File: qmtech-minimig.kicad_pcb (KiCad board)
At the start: 4 copper layers, 142.3 x 105.7 mm, 168 parts, among them IC1 ESP32-WROVER-B_(16MB), J1 DB9_Male, J10 DB23_Female_MountingHoles, J11 Conn_01x03_Male, J2 DB9_Male, J3 SCHA5B0200, J4 10118193-0001LF, J5 AUDIO-CONNECTOR-6P-SMD-344003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, J6 Mini-DIN-6, J7 Conn_02x13_Odd_Even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

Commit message: Add the missing files.
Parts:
- C11: value C -> 4u7F
- D3: footprint Diode_SMD:D_SMC -> Diode_SMD:D_SMA
- L5: footprint CDRH104RNP-220NC:INDPM102100X400N -> Inductor_SMD:L_Taiyo-Yuden_MD-4040
- SW1: value Reset ESP32 -> SW_Push
- moved C15 8.96 mm to (139.8, 136.3)
- moved C16 8.96 mm to (139.8, 138.3)
- moved JP1 8.96 mm to (147.6, 139.5)
- moved L5 5.91 mm to (134.6, 136.2)
- moved C11 4.16 mm to (104.8, 51.5), turned to 90 degrees
- moved R35 2.83 mm to (126.7, 144.1)
- moved R36 2.83 mm to (128.5, 144.1)
- moved R37 2.83 mm to (136.7, 144.2)
- moved U5 2.83 mm to (132.5, 144.0)
- moved D3 1.96 mm to (126.8, 136.0)
- moved R32 0.50 mm to (107.1, 46.8)
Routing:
- net Net-(C15-Pad1): track 32.9 -> 25.6 mm
- net VIN12V: track 130.5 -> 129.1 mm
- net VIN5V: track 224.7 -> 224.0 mm
- net ESP_SD_VCC_EN: track 60.3 -> 59.8 mm

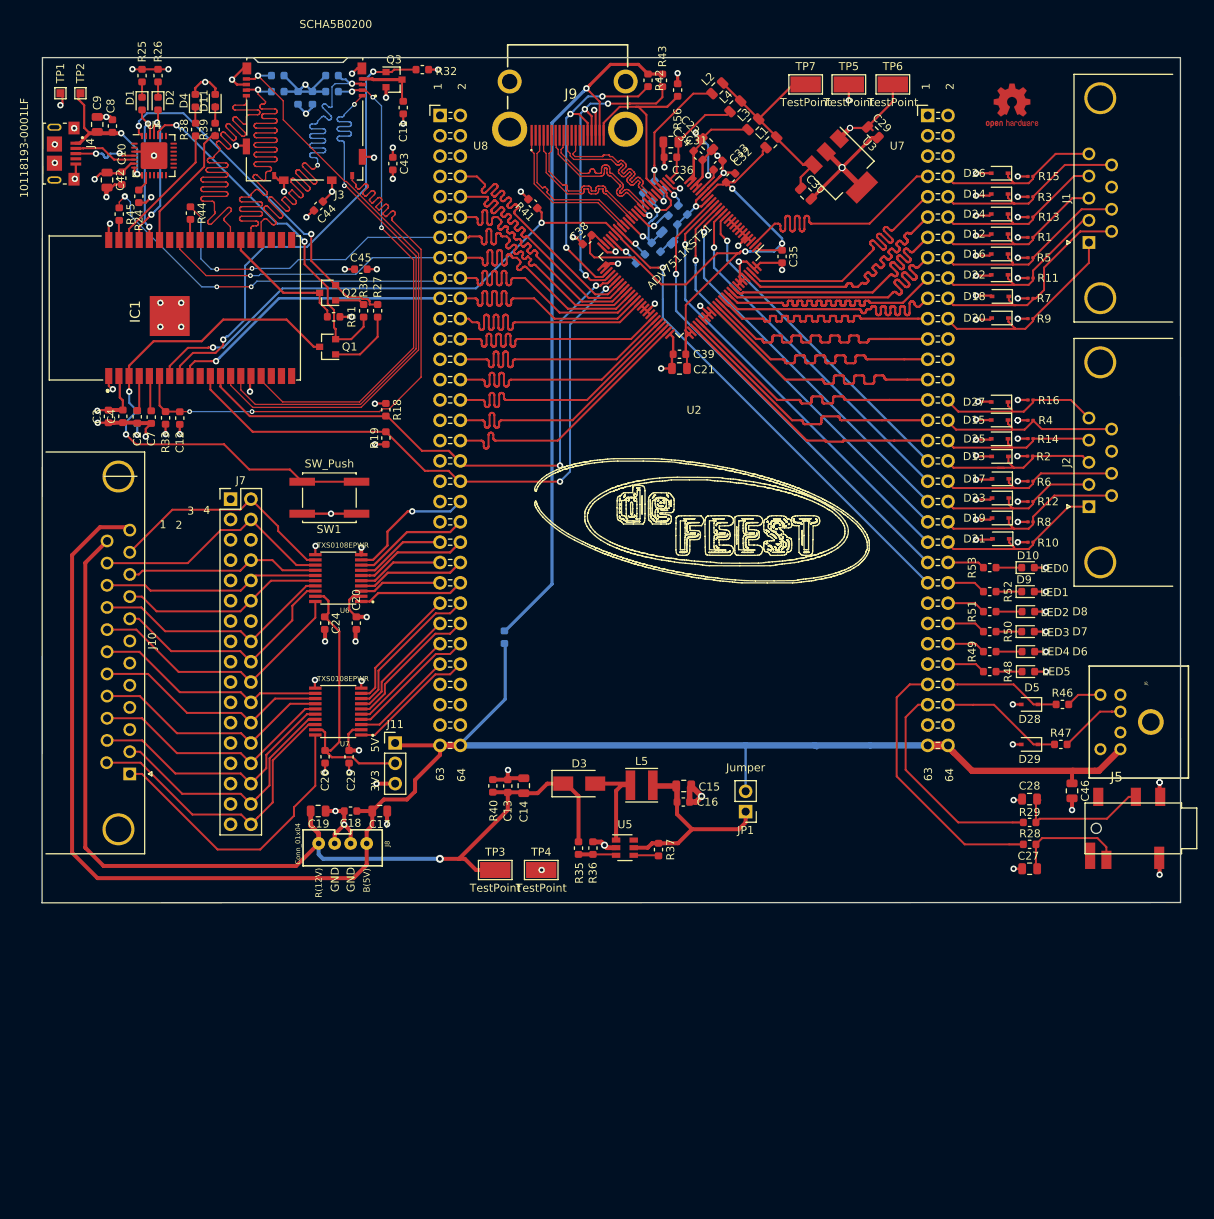
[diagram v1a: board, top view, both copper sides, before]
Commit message: Added ESD protection, and removed the curved lines around the adv7511.
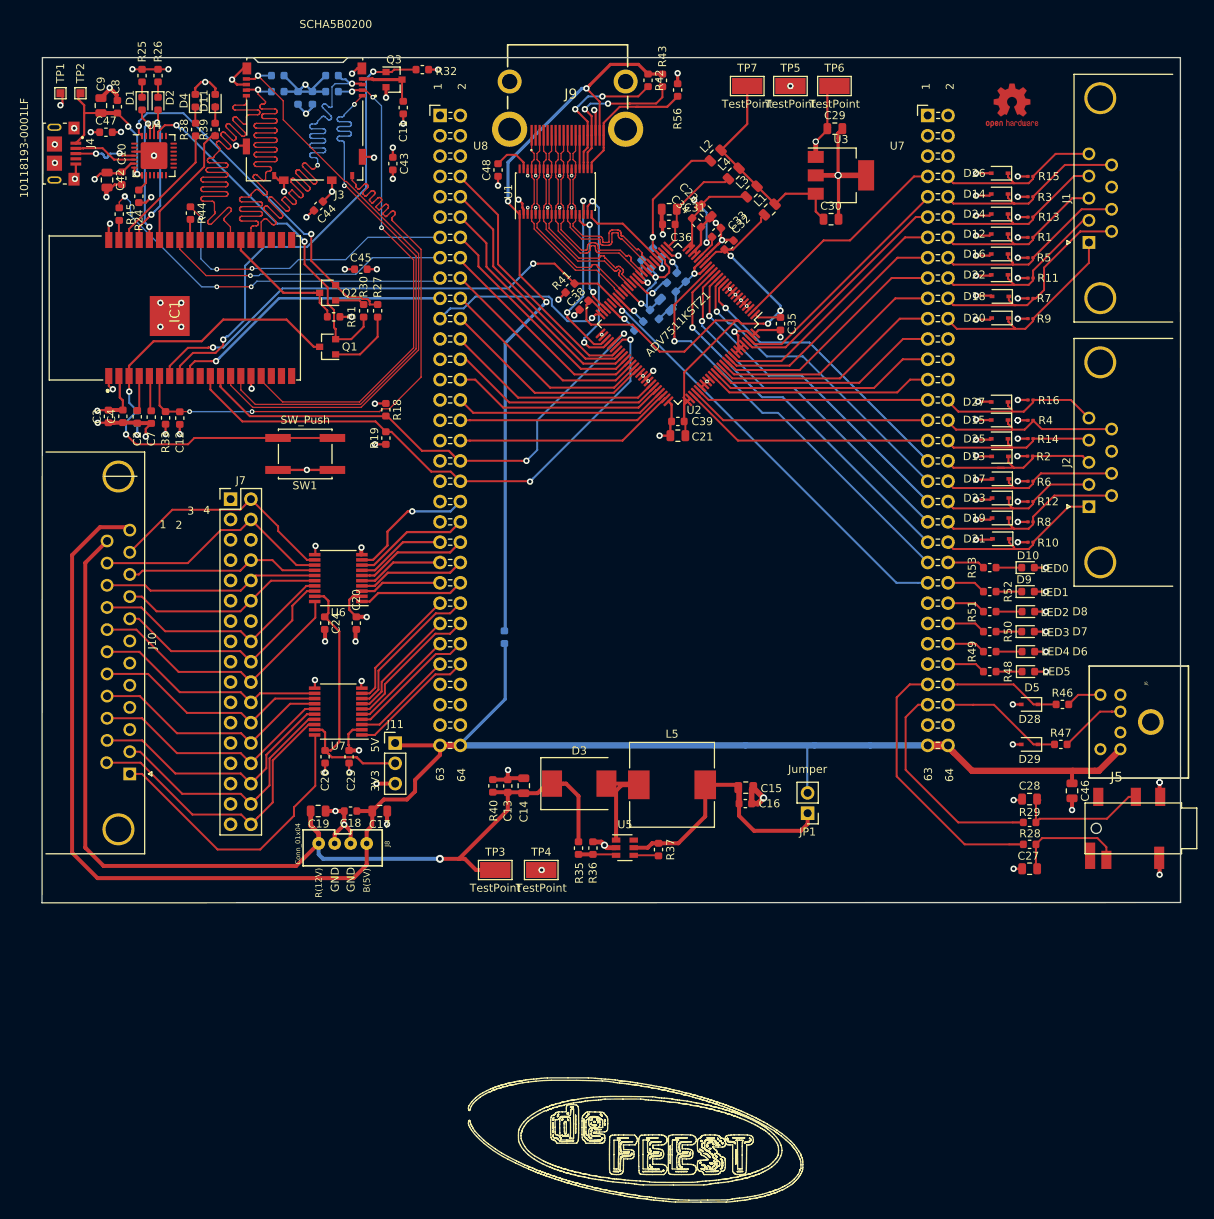
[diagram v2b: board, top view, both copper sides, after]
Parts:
- added C47: 10n, Capacitor_SMD:C_0603_1608Metric, F.Cu at (67.6, 54.6)
- added C48: 100nF, Resistor_SMD:R_0603_1608Metric, F.Cu at (116.6, 59.3)
- added U1: TPD12S520DBT, Package_SO:TSSOP-38_4.4x9.7mm_P0.5mm, F.Cu at (123.8, 62.0)
- C11: value 4u7F -> C
- D3: footprint Diode_SMD:D_SMA -> Diode_SMD:D_SMC
- L5: footprint Inductor_SMD:L_Taiyo-Yuden_MD-4040 -> Inductor_SMD:L_10.4x10.4_H4.8
- U6, U7: footprint TXS0108EPWR:SOP65P640X120-20N -> Package_SO:TSSOP-20_4.4x6.5mm_P0.65mm
- moved R41 11.5 mm to (125.6, 74.0), turned to 225 degrees
- moved C31 8.40 mm to (138.0, 64.2)
- moved C32 8.40 mm to (143.9, 67.1)
- moved C34 8.40 mm to (141.4, 65.9)
- moved C35 8.40 mm to (151.9, 78.5)
- moved C37 8.40 mm to (136.2, 77.4)
- moved C39 8.40 mm to (139.1, 90.7)
- moved L1 8.40 mm to (150.6, 64.2)
- moved L2 8.40 mm to (143.8, 57.5)
- moved L3 8.40 mm to (148.3, 62.0)
- moved L4 8.40 mm to (146.1, 59.7)
- moved R57 8.40 mm to (139.5, 72.7)
- moved C23 8.40 mm to (142.5, 64.5)
- moved C33 8.40 mm to (145.5, 68.7)
- moved C40 8.40 mm to (136.5, 69.6)
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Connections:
- net Net-(J9-Pad18) renamed /HDMI transmitter/HDMI5V
- ADV7511KSTZ1 pad 48: GND -> ADV_CEC
- ADV7511KSTZ1 pad 50: GND -> ADV_CECCLK
- J9 pad 13: Net-(J9-Pad13) -> ADV_CEC_C
- J9 pad 15: ADV_DDCSCL -> ADV_DDCSCL_C
- J9 pad 16: ADV_DDCSDA -> ADV_DDCSDA_C
- J9 pad 19: ADV_HPD -> ADV_HPD_C
- R42 pad 2: ADV_DDCSCL -> ADV_DDCSCL_C
- R43 pad 2: ADV_DDCSDA -> ADV_DDCSDA_C
- R56 pad 2: ADV_HPD -> ADV_HPD_C
- U2 pad U721: Net-(U2-PadU721) -> ADV_CECCLK
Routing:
- net ADV_CECCLK: track 0.00 -> 23.3 mm, vias 0 -> 1
- net ADV_DDCSDA_C: track 0.00 -> 19.9 mm, vias 0 -> 2
- net ADV_DDCSCL_C: track 0.00 -> 18.6 mm, vias 0 -> 2
- net ADV_HPD_C: track 0.00 -> 17.3 mm
- net ADV_DDCSDA: track 40.1 -> 24.3 mm, vias 3 -> 2
- net ADV_DDCSCL: track 39.2 -> 23.6 mm, vias 3 -> 2
- net ADV_CEC: track 0.00 -> 13.7 mm, vias 0 -> 2
- net ADV_HPD: track 24.0 -> 10.7 mm
- net ADV_INT: track 127.9 -> 118.1 mm
- net ADV_G_3: track 35.0 -> 26.6 mm
- net ADV_G_4: track 35.0 -> 26.6 mm
- net ADV_SCL: track 74.8 -> 66.5 mm
- net ADV_G_5: track 35.0 -> 27.0 mm
- net ADV_R_0: track 35.0 -> 27.1 mm
- net Net-(C15-Pad1): track 25.6 -> 33.4 mm
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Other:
- net class HDMI: clearance 0.2 -> 0.127; via_dia 0.4 -> 0.45
- rule via_min_drill: 0.3 -> 0.2
- rule via_min_size: 0.4 -> 0.45

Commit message: Add an oscillator for the CEC functionality.
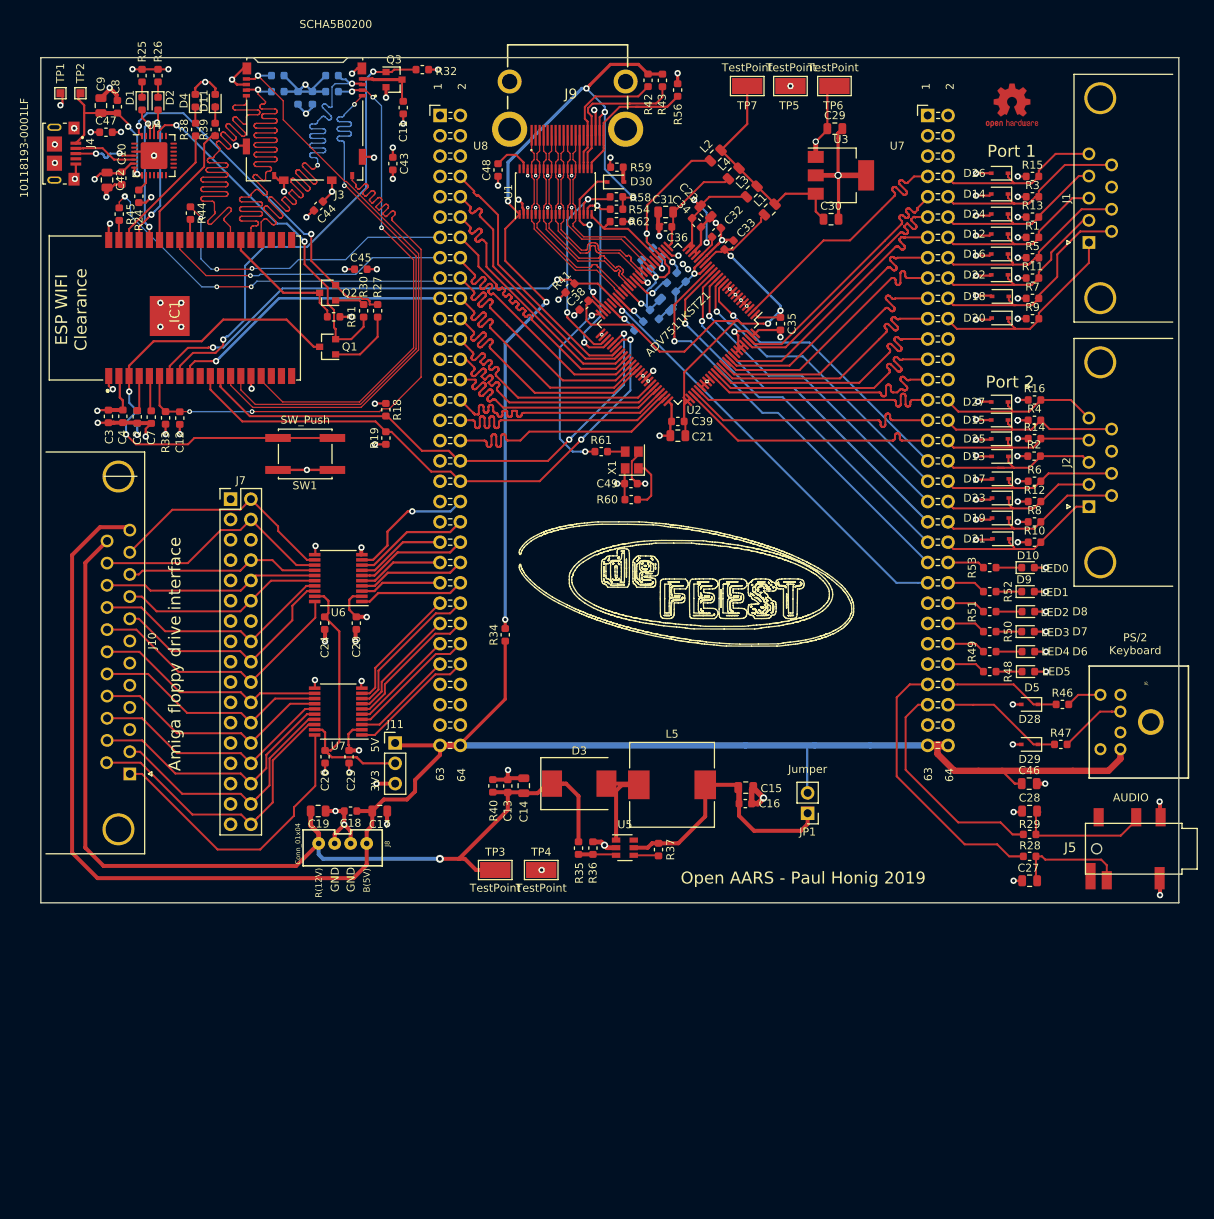
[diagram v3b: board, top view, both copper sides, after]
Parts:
- added C49: 100nF, Capacitor_SMD:C_0603_1608Metric, F.Cu at (133.2, 98.5)
- added D30: 1N4148, Diode_SMD:D_SOD-323, F.Cu at (131.3, 60.8)
- added R54: 2K, Resistor_SMD:R_0603_1608Metric, F.Cu at (131.4, 64.2)
- added R58: 2K, Resistor_SMD:R_0603_1608Metric, F.Cu at (131.4, 62.6)
- added R59: 27k, Resistor_SMD:R_0603_1608Metric, F.Cu at (131.5, 59.0)
- added R60: 10k, Resistor_SMD:R_0603_1608Metric, F.Cu at (133.2, 100.5)
- added R61: 27, Resistor_SMD:R_0603_1608Metric, F.Cu at (129.5, 94.5)
- added R62: 10k, Resistor_SMD:R_0603_1608Metric, F.Cu at (131.4, 65.8)
- added X1: MCSJK-3N-16.00-3.3-50-B, Oscillator:Oscillator_SMD_Abracon_ASE-4Pin_3.2x2.5mm, F.Cu at (133.3, 95.5)
- R1, R10, R11, R12, R13, R14, R15, R16, R2, R3, R4, R5, R6, R7, R8, R9: footprint Resistor_SMD:R_0201_0603Metric -> Resistor_SMD:R_0603_1608Metric
- R34: moved to F.Cu
- moved C46 5.43 mm to (183.0, 136.0), turned to 0 degrees
- moved J5 2.55 mm to (197.0, 144.1)
- moved C27 1.50 mm to (183.1, 148.1)
- moved C28 1.50 mm to (183.0, 139.4)
- moved R28 1.50 mm to (183.1, 145.1)
- moved R29 1.50 mm to (183.1, 142.4)
- moved C31 0.57 mm to (137.6, 64.5)
- moved C36 0.51 mm to (137.5, 66.4)
- moved R10 0.50 mm to (183.7, 105.8)
- moved R12 0.50 mm to (183.7, 100.7)
- moved R14 0.50 mm to (183.7, 92.9)
- moved R16 0.50 mm to (183.7, 88.0)
- moved R2 0.50 mm to (183.6, 95.1)
- moved R4 0.50 mm to (183.7, 90.6)
- moved R6 0.50 mm to (183.7, 98.2)
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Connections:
- U2 pad U721: ADV_CECCLK -> Net-(U2-PadU721)
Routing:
- net /HDMI transmitter/HDMI5V: track 94.1 -> 111.1 mm, vias 3 -> 6
- net Net-(R60-Pad2): track 0.00 -> 6.61 mm
- net ADV_G_3: track 26.6 -> 33.0 mm
- net ADV_G_4: track 26.6 -> 32.9 mm
- net ADV_CEC: track 13.7 -> 19.9 mm
- net GND: track 361.2 -> 367.3 mm, vias 105 -> 108
- net ADV_G_5: track 27.0 -> 33.0 mm
- net ADV_R_0: track 27.1 -> 33.0 mm
- net 3V3: track 181.4 -> 187.1 mm, vias 48 -> 50
- net ADV_G_6: track 27.3 -> 33.0 mm
- net ADV_R_1: track 27.4 -> 33.0 mm
- net ADV_R_2: track 27.5 -> 33.0 mm
- net ADV_G_7: track 27.7 -> 33.1 mm
- net ADV_G_2: track 27.8 -> 33.0 mm
- net ADV_R_3: track 28.0 -> 33.0 mm
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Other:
- board size 142.3 x 105.7 mm -> 142.2 x 105.7 mm
- board text added: "105mm"
- board text added: "142mm"
- board text added: "AUDIO"
- board text added: "Amiga floppy drive interface"
- board text added: "ESP WIFI Clearance"
- board text added: "Open AARS - Paul Honig 2019"
- board text added: "PS/2 Keyboard"
- board text added: "Port 1"
- board text added: "Port 2"
- board text removed: "1"
- board text removed: "2"
- board text removed: "3"
- board text removed: "4"

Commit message: Added mounting holes.
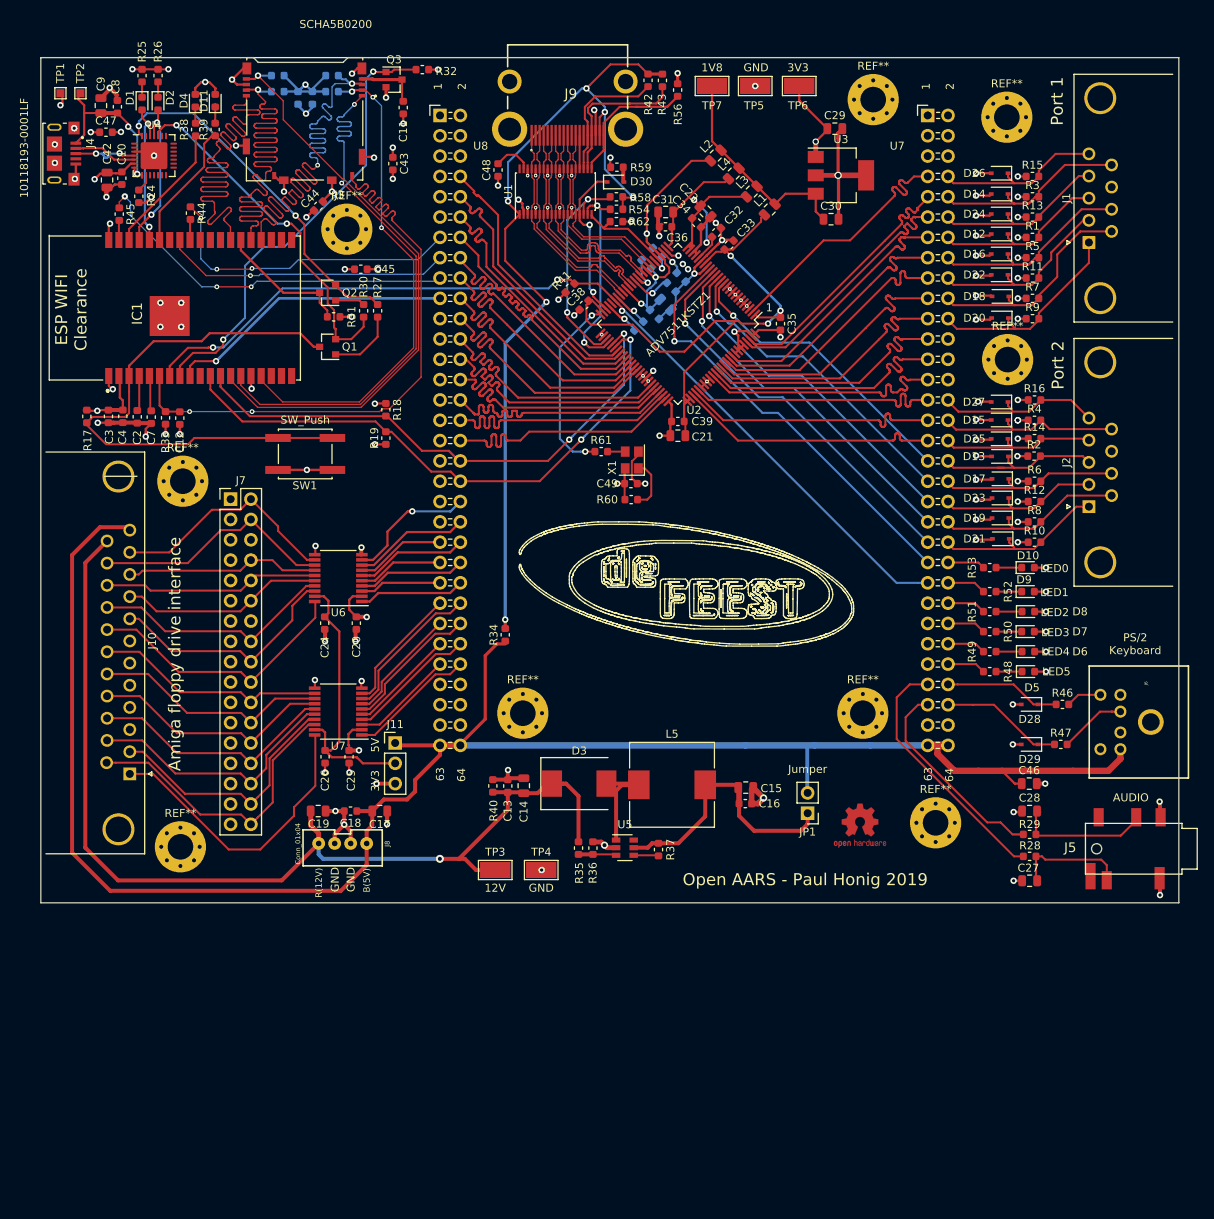
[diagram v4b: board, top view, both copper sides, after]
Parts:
- added REF**: MountingHole_3.2mm_M3_Pad_Via, MountingHole:MountingHole_3.2mm_M3_Pad_Via, F.Cu at (180.2, 52.7)
- added REF**: MountingHole_3.2mm_M3_Pad_Via, MountingHole:MountingHole_3.2mm_M3_Pad_Via, F.Cu at (119.7, 127.2)
- added REF**: MountingHole_3.2mm_M3_Pad_Via, MountingHole:MountingHole_3.2mm_M3_Pad_Via, F.Cu at (162.2, 127.2)
- added REF**: MountingHole_3.2mm_M3_Pad_Via, MountingHole:MountingHole_3.2mm_M3_Pad_Via, F.Cu at (180.3, 83.0)
- added REF**: MountingHole_3.2mm_M3_Pad_Via, MountingHole:MountingHole_3.2mm_M3_Pad_Via, F.Cu at (97.7, 66.7)
- added REF**: MountingHole_3.2mm_M3_Pad_Via, MountingHole:MountingHole_3.2mm_M3_Pad_Via, F.Cu at (163.5, 50.5)
- added REF**: MountingHole_3.2mm_M3_Pad_Via, MountingHole:MountingHole_3.2mm_M3_Pad_Via, F.Cu at (171.3, 140.9)
- added REF**: MountingHole_3.2mm_M3_Pad_Via, MountingHole:MountingHole_3.2mm_M3_Pad_Via, F.Cu at (76.9, 143.9)
- added REF**: MountingHole_3.2mm_M3_Pad_Via, MountingHole:MountingHole_3.2mm_M3_Pad_Via, F.Cu at (77.2, 98.2)
- R17: moved to F.Cu
- TP3: value TestPoint -> 12V
- TP4, TP5: value TestPoint -> GND
- TP6: value TestPoint -> 3V3
- TP7: value TestPoint -> 1V8
- moved REF** 92.0 mm to (161.8, 141.2)
- moved R17 6.30 mm to (65.2, 90.1), turned to 270 degrees
- moved TP5 4.40 mm to (148.8, 48.8)
- moved TP6 4.40 mm to (154.2, 48.8)
- moved TP7 4.40 mm to (143.3, 48.8)
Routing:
- net ESP_RST: track 63.8 -> 69.9 mm, vias 2 -> 0
- net AUDIO_LEFT: track 34.4 -> 31.7 mm
- net AUDIO_RIGHT: track 28.0 -> 25.9 mm
- net VIN5V: track 227.8 -> 229.8 mm
- net ESP_SD_VCC_EN: track 59.8 -> 58.0 mm
- net 3V3: track 187.1 -> 188.7 mm, vias 50 -> 49
- net VIN12V: track 129.1 -> 130.6 mm
- net /HDMI transmitter/1V8: track 29.8 -> 29.0 mm
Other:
- board text added: "1"
- board text added: "Paul Honig (paul@scene.rs) deFEEST retro entertainment 2019 Version: 0.001 CERN Open Hardware Licence"
- board text removed: "Paul Honig (paul@scene.rs) deFEEST retro entertainment 2019 Version: 0.500 CERN Open Hardware Licence"
